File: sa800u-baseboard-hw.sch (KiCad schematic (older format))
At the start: 4 parts

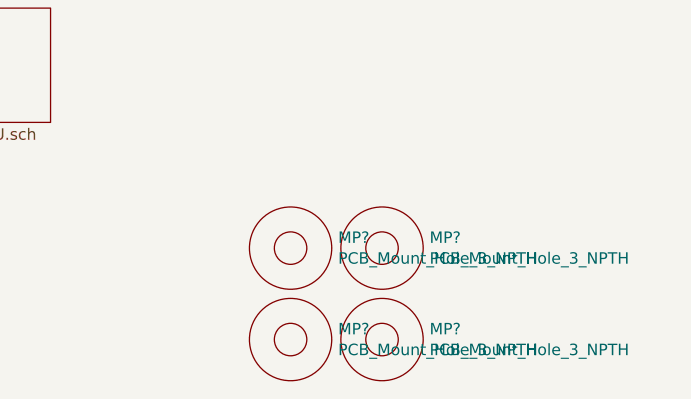
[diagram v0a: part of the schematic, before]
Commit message: added holes on schematic
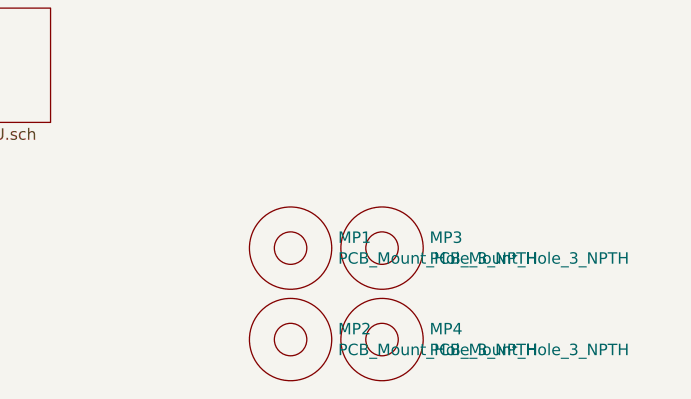
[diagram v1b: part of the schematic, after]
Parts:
- gave numbers to parts that had none: 4
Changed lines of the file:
@@
 $EndSheet
 $Comp
-L antmicroMechanicalParts:PCB_Mount_Hole_3_NPTH MP?
+L antmicroMechanicalParts:PCB_Mount_Hole_3_NPTH MP1
 U 1 1 61B52107
 P 12050 8050
-F 0 "MP?" H 12258 8096 50  0000 L CNN
+F 0 "MP1" H 12258 8096 50  0000 L CNN
 F 1 "PCB_Mount_Hole_3_NPTH" H 12258 8005 50  0000 L CNN
 F 2 "antmicro-footprints:mounting-hole-3mm-NPTH" H 12850 8750 50  0001 C CNN
@@
 $EndComp
 $Comp
-L antmicroMechanicalParts:PCB_Mount_Hole_3_NPTH MP?
+L antmicroMechanicalParts:PCB_Mount_Hole_3_NPTH MP3
 U 1 1 61B52579
 P 12450 8050
-F 0 "MP?" H 12658 8096 50  0000 L CNN
+F 0 "MP3" H 12658 8096 50  0000 L CNN
 F 1 "PCB_Mount_Hole_3_NPTH" H 12658 8005 50  0000 L CNN
 F 2 "antmicro-footprints:mounting-hole-3mm-NPTH" H 13250 8750 50  0001 C CNN
@@
 $EndComp
 $Comp
-L antmicroMechanicalParts:PCB_Mount_Hole_3_NPTH MP?
+L antmicroMechanicalParts:PCB_Mount_Hole_3_NPTH MP2
 U 1 1 61B52868
 P 12050 8450
-F 0 "MP?" H 12258 8496 50  0000 L CNN
+F 0 "MP2" H 12258 8496 50  0000 L CNN
 F 1 "PCB_Mount_Hole_3_NPTH" H 12258 8405 50  0000 L CNN
 F 2 "antmicro-footprints:mounting-hole-3mm-NPTH" H 12850 9150 50  0001 C CNN
@@
 $EndComp
 $Comp
-L antmicroMechanicalParts:PCB_Mount_Hole_3_NPTH MP?
+L antmicroMechanicalParts:PCB_Mount_Hole_3_NPTH MP4
 U 1 1 61B52B11
 P 12450 8450
-F 0 "MP?" H 12658 8496 50  0000 L CNN
+F 0 "MP4" H 12658 8496 50  0000 L CNN
 F 1 "PCB_Mount_Hole_3_NPTH" H 12658 8405 50  0000 L CNN
 F 2 "antmicro-footprints:mounting-hole-3mm-NPTH" H 13250 9150 50  0001 C CNN

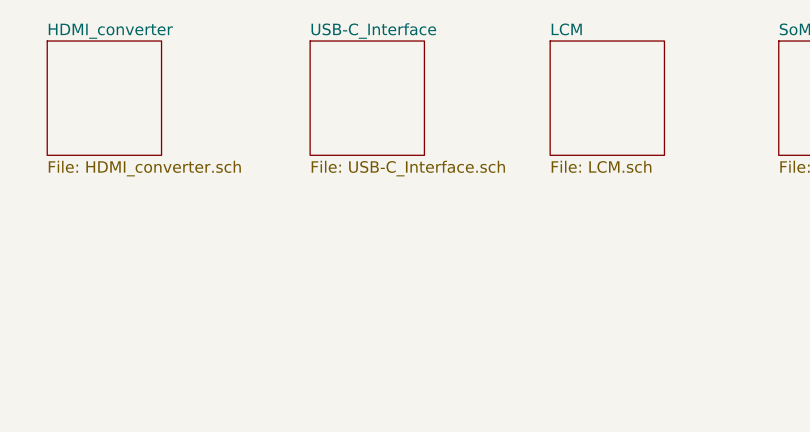
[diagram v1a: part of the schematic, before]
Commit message: implementing usb muxes and current limiter
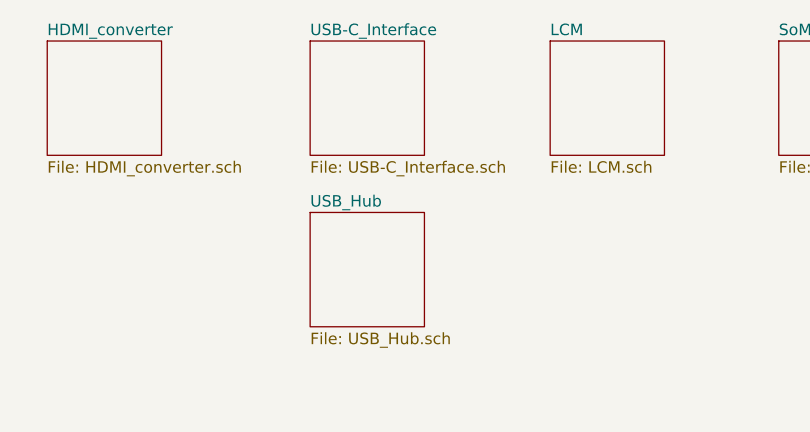
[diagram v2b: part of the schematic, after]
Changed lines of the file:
@@
 $Descr A3 16535 11693
 encoding utf-8
-Sheet 1 11
+Sheet 1 12
 Title ""
 Date ""
@@
 	1    0    0    -1
 $EndComp
+$Sheet
+S 4150 7750 500  500
+U 628CDA4A
+F0 "USB_Hub" 50
+F1 "USB_Hub.sch" 50
+$EndSheet
 $EndSCHEMATC

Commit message: added usb c controller and mux, removed hub
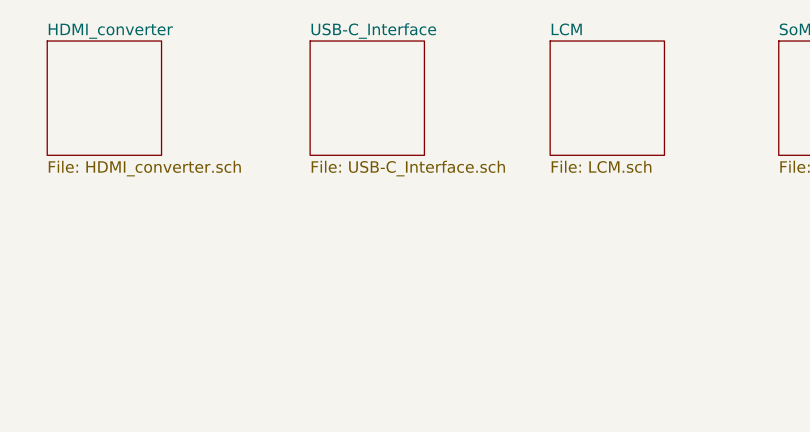
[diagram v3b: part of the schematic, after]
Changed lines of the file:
@@
 $Descr A3 16535 11693
 encoding utf-8
-Sheet 1 12
+Sheet 1 11
 Title ""
 Date ""
@@
 	1    0    0    -1
 $EndComp
-$Sheet
-S 4150 7750 500  500
-U 628CDA4A
-F0 "USB_Hub" 50
-F1 "USB_Hub.sch" 50
-$EndSheet
 $EndSCHEMATC

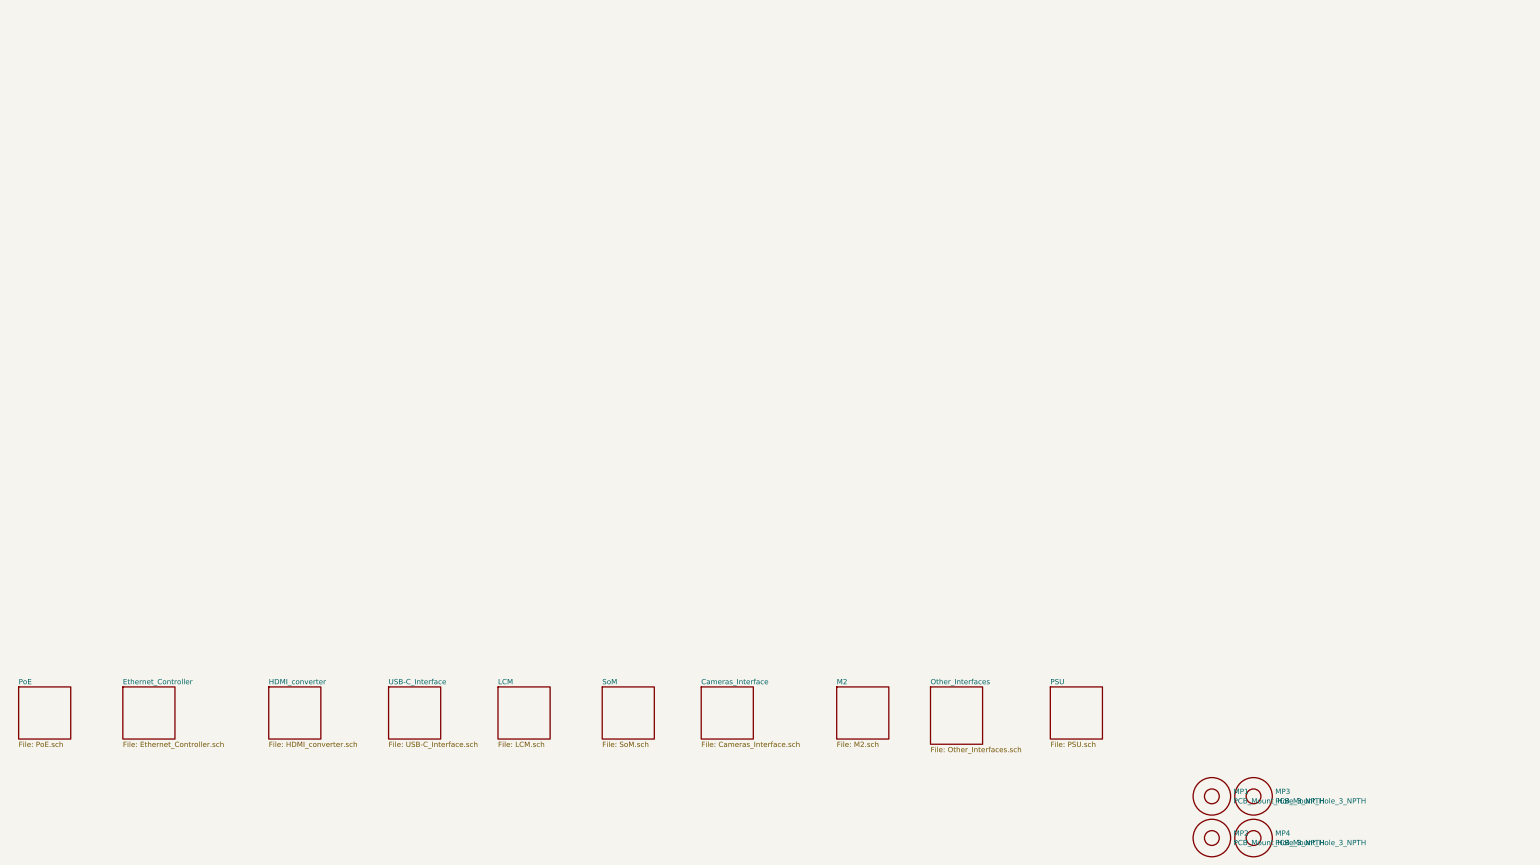
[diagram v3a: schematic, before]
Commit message: changed arrangement of hierarchical sheets
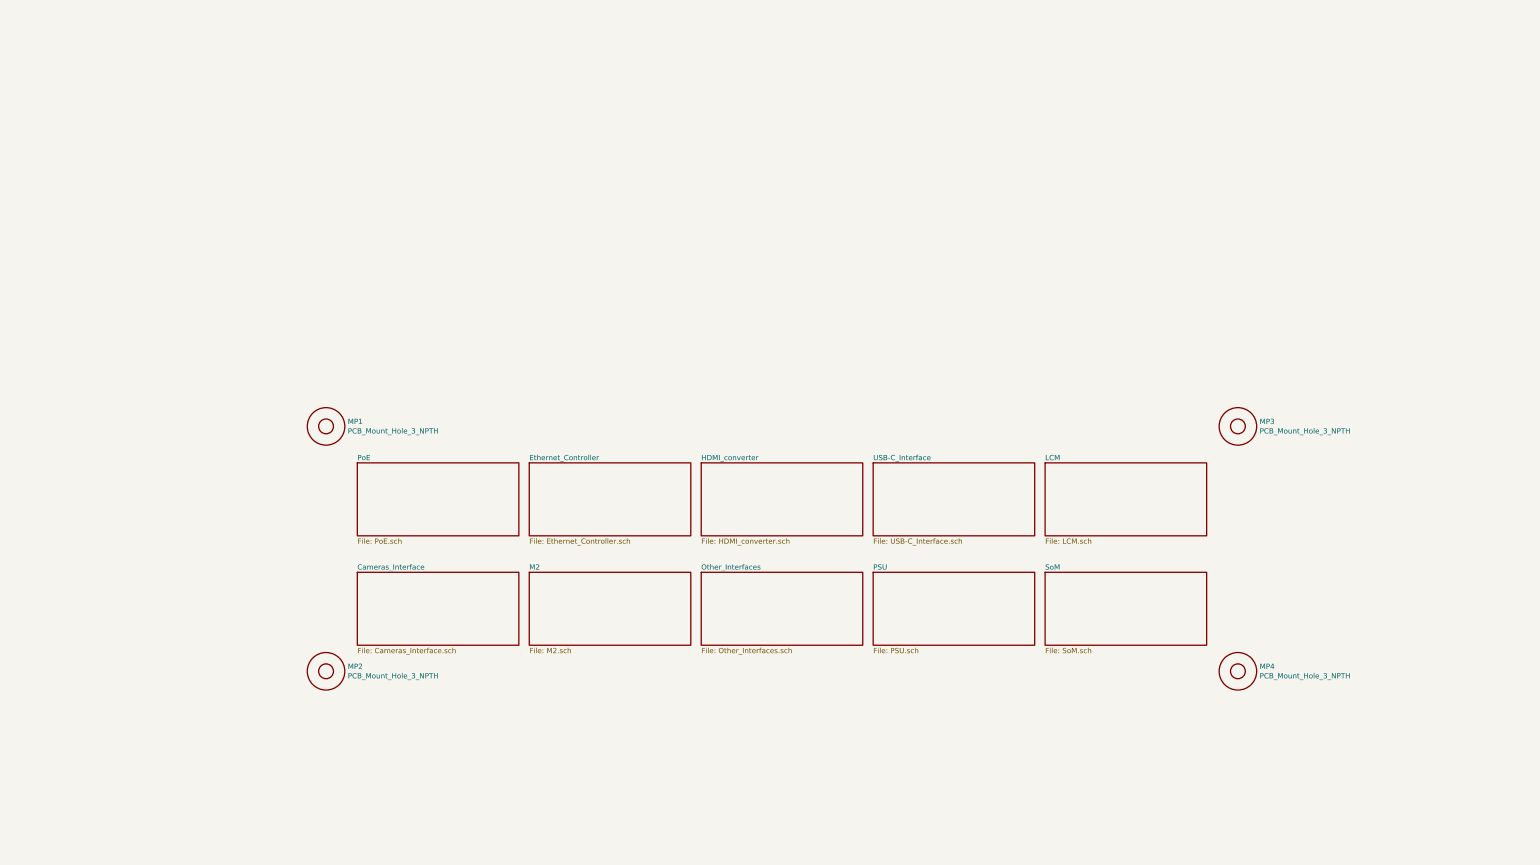
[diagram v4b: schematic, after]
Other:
- moved on the sheet: MP1, MP2, MP3, MP4
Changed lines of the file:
@@
 $EndDescr
 $Sheet
-S 1600 7000 500  500
+S 5500 4850 1550 700
 U 618E716E
 F0 "Ethernet_Controller" 50
@@
 $EndSheet
 $Sheet
-S 3000 7000 500  500
+S 7150 4850 1550 700
 U 6197686D
 F0 "HDMI_converter" 50
@@
 $EndSheet
 $Sheet
-S 4150 7000 500  500
+S 8800 4850 1550 700
 U 61A2F307
 F0 "USB-C_Interface " 50
@@
 $EndSheet
 $Sheet
-S 5200 7000 500  500
+S 10450 4850 1550 700
 U 61BD2CC1
 F0 "LCM" 50
@@
 $EndSheet
 $Sheet
-S 600  7000 500  500
-U 61A19323
-F0 "PoE" 50
-F1 "PoE.sch" 50
-$EndSheet
-$Sheet
-S 6200 7000 500  500
+S 10450 5900 1550 700
 U 61A4BC4F
 F0 "SoM" 50
@@
 $EndSheet
 $Sheet
-S 7150 7000 500  500
+S 3850 5900 1550 700
 U 61A60486
 F0 "Cameras_Interface" 50
@@
 $EndSheet
 $Sheet
-S 8450 7000 500  500
+S 5500 5900 1550 700
 U 61B13669
 F0 "M2" 50
@@
 $EndSheet
 $Sheet
-S 9350 7000 500  550
+S 7150 5900 1550 700
 U 61C01D88
 F0 "Other_Interfaces" 50
@@
 $EndSheet
 $Sheet
-S 10500 7000 500  500
+S 8800 5900 1550 700
 U 61B0DC30
 F0 "PSU" 50
@@
 L antmicroMechanicalParts:PCB_Mount_Hole_3_NPTH MP1
 U 1 1 61B52107
-P 12050 8050
-F 0 "MP1" H 12258 8096 50  0000 L CNN
-F 1 "PCB_Mount_Hole_3_NPTH" H 12258 8005 50  0000 L CNN
-F 2 "antmicro-footprints:mounting-hole-3mm-NPTH" H 12850 8750 50  0001 C CNN
-F 3 "" H 13000 8850 50  0001 C CNN
-	1    12050 8050
+P 3550 4500
+F 0 "MP1" H 3758 4546 50  0000 L CNN
+F 1 "PCB_Mount_Hole_3_NPTH" H 3758 4455 50  0000 L CNN
+F 2 "antmicro-footprints:mounting-hole-3mm-NPTH" H 4350 5200 50  0001 C CNN
+F 3 "" H 4500 5300 50  0001 C CNN
+	1    3550 4500
 	1    0    0    -1
 $EndComp
@@
 L antmicroMechanicalParts:PCB_Mount_Hole_3_NPTH MP3
 U 1 1 61B52579
-P 12450 8050
-F 0 "MP3" H 12658 8096 50  0000 L CNN
-F 1 "PCB_Mount_Hole_3_NPTH" H 12658 8005 50  0000 L CNN
-F 2 "antmicro-footprints:mounting-hole-3mm-NPTH" H 13250 8750 50  0001 C CNN
-F 3 "" H 13400 8850 50  0001 C CNN
-	1    12450 8050
+P 12300 4500
+F 0 "MP3" H 12508 4546 50  0000 L CNN
+F 1 "PCB_Mount_Hole_3_NPTH" H 12508 4455 50  0000 L CNN
+F 2 "antmicro-footprints:mounting-hole-3mm-NPTH" H 13100 5200 50  0001 C CNN
+F 3 "" H 13250 5300 50  0001 C CNN
+	1    12300 4500
 	1    0    0    -1
 $EndComp
@@
 L antmicroMechanicalParts:PCB_Mount_Hole_3_NPTH MP2
 U 1 1 61B52868
-P 12050 8450
-F 0 "MP2" H 12258 8496 50  0000 L CNN
-F 1 "PCB_Mount_Hole_3_NPTH" H 12258 8405 50  0000 L CNN
-F 2 "antmicro-footprints:mounting-hole-3mm-NPTH" H 12850 9150 50  0001 C CNN
-F 3 "" H 13000 9250 50  0001 C CNN
-	1    12050 8450
+P 3550 6850
+F 0 "MP2" H 3758 6896 50  0000 L CNN
+F 1 "PCB_Mount_Hole_3_NPTH" H 3758 6805 50  0000 L CNN
+F 2 "antmicro-footprints:mounting-hole-3mm-NPTH" H 4350 7550 50  0001 C CNN
+F 3 "" H 4500 7650 50  0001 C CNN
+	1    3550 6850
 	1    0    0    -1
 $EndComp
@@
 L antmicroMechanicalParts:PCB_Mount_Hole_3_NPTH MP4
 U 1 1 61B52B11
-P 12450 8450
-F 0 "MP4" H 12658 8496 50  0000 L CNN
-F 1 "PCB_Mount_Hole_3_NPTH" H 12658 8405 50  0000 L CNN
-F 2 "antmicro-footprints:mounting-hole-3mm-NPTH" H 13250 9150 50  0001 C CNN
-F 3 "" H 13400 9250 50  0001 C CNN
-	1    12450 8450
+P 12300 6850
+F 0 "MP4" H 12508 6896 50  0000 L CNN
+F 1 "PCB_Mount_Hole_3_NPTH" H 12508 6805 50  0000 L CNN
+F 2 "antmicro-footprints:mounting-hole-3mm-NPTH" H 13100 7550 50  0001 C CNN
+F 3 "" H 13250 7650 50  0001 C CNN
+	1    12300 6850
 	1    0    0    -1
 $EndComp
+$Sheet
+S 3850 4850 1550 700
+U 61A19323
+F0 "PoE" 50
+F1 "PoE.sch" 50
+$EndSheet
 $EndSCHEMATC

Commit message: Add review comments
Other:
- note added: "Use 6mm spacers insted of PCB mounting holes.\nThis will allow to put device on a desk without risking \ndamage to components on the bottom of the board \nAlternatively add space for screw head/spacer on PCB\n(ie. MP1 will interfere with connector when using screw/spacer)"
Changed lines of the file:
@@
 F1 "PoE.sch" 50
 $EndSheet
+Text Notes 12100 4275 0    50   ~ 0
+Use 6mm spacers insted of PCB mounting holes.\nThis will allow to put device on a desk without risking \ndamage to components on the bottom of the board \nAlternatively add space for screw head/spacer on PCB\n(ie. MP1 will interfere with connector when using screw/spacer)
 $EndSCHEMATC

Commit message: Add local libs to fix CI
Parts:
- MP1, MP2, MP3, MP4: footprint antmicro-footprints:mounting-hole-3mm-NPTH -> sa800u-baseboard-hw-footprints:mounting-hole-3mm-NPTH; symbol antmicroMechanicalParts:PCB_Mount_Hole_3_NPTH -> sa800u-baseboard-hw:PCB_Mount_Hole_3_NPTH
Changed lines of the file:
@@
 $EndSheet
 $Comp
-L antmicroMechanicalParts:PCB_Mount_Hole_3_NPTH MP1
+L sa800u-baseboard-hw:PCB_Mount_Hole_3_NPTH MP1
 U 1 1 61B52107
 P 3550 4500
 F 0 "MP1" H 3758 4546 50  0000 L CNN
 F 1 "PCB_Mount_Hole_3_NPTH" H 3758 4455 50  0000 L CNN
-F 2 "antmicro-footprints:mounting-hole-3mm-NPTH" H 4350 5200 50  0001 C CNN
+F 2 "sa800u-baseboard-hw-footprints:mounting-hole-3mm-NPTH" H 4350 5200 50  0001 C CNN
 F 3 "" H 4500 5300 50  0001 C CNN
 	1    3550 4500
@@
 $EndComp
 $Comp
-L antmicroMechanicalParts:PCB_Mount_Hole_3_NPTH MP3
+L sa800u-baseboard-hw:PCB_Mount_Hole_3_NPTH MP3
 U 1 1 61B52579
 P 12300 4500
 F 0 "MP3" H 12508 4546 50  0000 L CNN
 F 1 "PCB_Mount_Hole_3_NPTH" H 12508 4455 50  0000 L CNN
-F 2 "antmicro-footprints:mounting-hole-3mm-NPTH" H 13100 5200 50  0001 C CNN
+F 2 "sa800u-baseboard-hw-footprints:mounting-hole-3mm-NPTH" H 13100 5200 50  0001 C CNN
 F 3 "" H 13250 5300 50  0001 C CNN
 	1    12300 4500
@@
 $EndComp
 $Comp
-L antmicroMechanicalParts:PCB_Mount_Hole_3_NPTH MP2
+L sa800u-baseboard-hw:PCB_Mount_Hole_3_NPTH MP2
 U 1 1 61B52868
 P 3550 6850
 F 0 "MP2" H 3758 6896 50  0000 L CNN
 F 1 "PCB_Mount_Hole_3_NPTH" H 3758 6805 50  0000 L CNN
-F 2 "antmicro-footprints:mounting-hole-3mm-NPTH" H 4350 7550 50  0001 C CNN
+F 2 "sa800u-baseboard-hw-footprints:mounting-hole-3mm-NPTH" H 4350 7550 50  0001 C CNN
 F 3 "" H 4500 7650 50  0001 C CNN
 	1    3550 6850
@@
 $EndComp
 $Comp
-L antmicroMechanicalParts:PCB_Mount_Hole_3_NPTH MP4
+L sa800u-baseboard-hw:PCB_Mount_Hole_3_NPTH MP4
 U 1 1 61B52B11
 P 12300 6850
 F 0 "MP4" H 12508 6896 50  0000 L CNN
 F 1 "PCB_Mount_Hole_3_NPTH" H 12508 6805 50  0000 L CNN
-F 2 "antmicro-footprints:mounting-hole-3mm-NPTH" H 13100 7550 50  0001 C CNN
+F 2 "sa800u-baseboard-hw-footprints:mounting-hole-3mm-NPTH" H 13100 7550 50  0001 C CNN
 F 3 "" H 13250 7650 50  0001 C CNN
 	1    12300 6850
